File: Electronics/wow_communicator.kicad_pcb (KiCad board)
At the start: 2 copper layers, 5 parts, among them SW1 SW_SPST, SW2 SW_SPST, U1 STM32C011F6Px

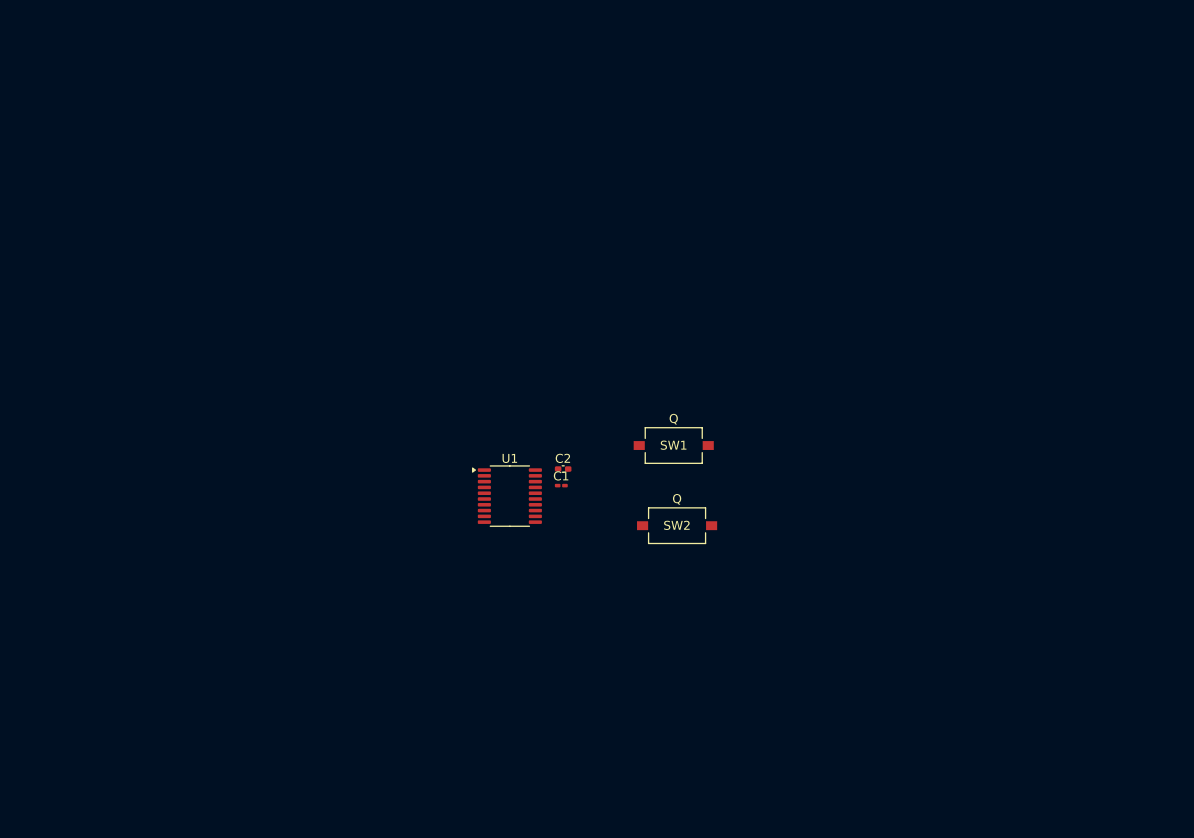
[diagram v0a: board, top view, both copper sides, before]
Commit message: arranged keys for keyboard. marked out lcd
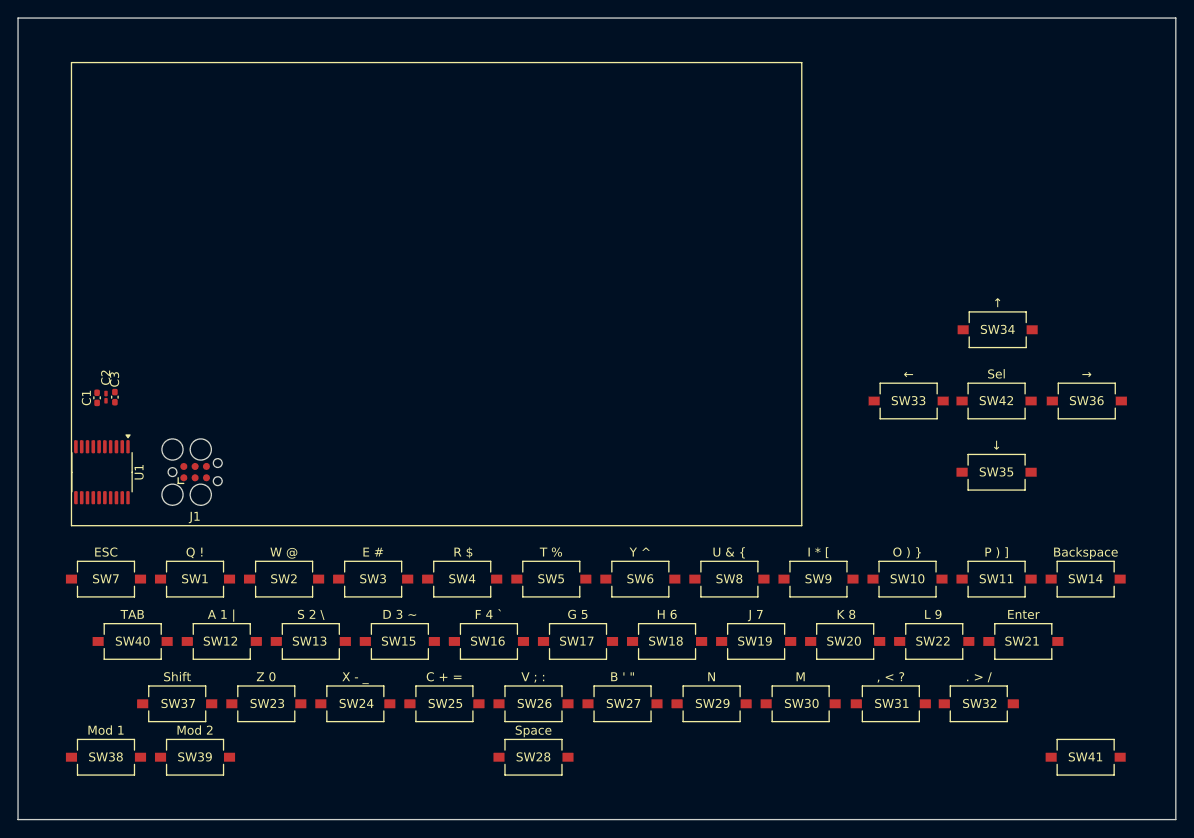
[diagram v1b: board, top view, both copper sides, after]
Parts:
- added C1: 100n, Capacitor_SMD:C_0402_1005Metric_Pad0.74x0.62mm_HandSolder, F.Cu at (93.9, 92.6)
- added J1: DEBUG, Connector:Tag-Connect_TC2030-IDC-FP_2x03_P1.27mm_Vertical, F.Cu at (104.9, 101.0)
- added SW10: SW_SPST, Button_Switch_SMD:SW_Tactile_SPST_NO_Straight_CK_PTS636Sx25SMTRLFS, F.Cu at (184.9, 113.0)
- added SW11: SW_SPST, Button_Switch_SMD:SW_Tactile_SPST_NO_Straight_CK_PTS636Sx25SMTRLFS, F.Cu at (194.9, 113.0)
- added SW12: SW_SPST, Button_Switch_SMD:SW_Tactile_SPST_NO_Straight_CK_PTS636Sx25SMTRLFS, F.Cu at (107.9, 120.0)
- added SW13: SW_SPST, Button_Switch_SMD:SW_Tactile_SPST_NO_Straight_CK_PTS636Sx25SMTRLFS, F.Cu at (117.9, 120.0)
- added SW14: SW_SPST, Button_Switch_SMD:SW_Tactile_SPST_NO_Straight_CK_PTS636Sx25SMTRLFS, F.Cu at (204.9, 113.0)
- added SW15: SW_SPST, Button_Switch_SMD:SW_Tactile_SPST_NO_Straight_CK_PTS636Sx25SMTRLFS, F.Cu at (127.9, 120.0)
- added SW16: SW_SPST, Button_Switch_SMD:SW_Tactile_SPST_NO_Straight_CK_PTS636Sx25SMTRLFS, F.Cu at (137.9, 120.0)
- added SW17: SW_SPST, Button_Switch_SMD:SW_Tactile_SPST_NO_Straight_CK_PTS636Sx25SMTRLFS, F.Cu at (147.9, 120.0)
- added SW18: SW_SPST, Button_Switch_SMD:SW_Tactile_SPST_NO_Straight_CK_PTS636Sx25SMTRLFS, F.Cu at (157.9, 120.0)
- added SW19: SW_SPST, Button_Switch_SMD:SW_Tactile_SPST_NO_Straight_CK_PTS636Sx25SMTRLFS, F.Cu at (167.9, 120.0)
- added SW20: SW_SPST, Button_Switch_SMD:SW_Tactile_SPST_NO_Straight_CK_PTS636Sx25SMTRLFS, F.Cu at (177.9, 120.0)
- added SW21: SW_SPST, Button_Switch_SMD:SW_Tactile_SPST_NO_Straight_CK_PTS636Sx25SMTRLFS, F.Cu at (197.9, 120.0)
- added SW22: SW_SPST, Button_Switch_SMD:SW_Tactile_SPST_NO_Straight_CK_PTS636Sx25SMTRLFS, F.Cu at (187.9, 120.0)
- added SW23: SW_SPST, Button_Switch_SMD:SW_Tactile_SPST_NO_Straight_CK_PTS636Sx25SMTRLFS, F.Cu at (112.9, 127.0)
- added SW24: SW_SPST, Button_Switch_SMD:SW_Tactile_SPST_NO_Straight_CK_PTS636Sx25SMTRLFS, F.Cu at (122.9, 127.0)
- added SW25: SW_SPST, Button_Switch_SMD:SW_Tactile_SPST_NO_Straight_CK_PTS636Sx25SMTRLFS, F.Cu at (132.9, 127.0)
- added SW26: SW_SPST, Button_Switch_SMD:SW_Tactile_SPST_NO_Straight_CK_PTS636Sx25SMTRLFS, F.Cu at (142.9, 127.0)
- added SW27: SW_SPST, Button_Switch_SMD:SW_Tactile_SPST_NO_Straight_CK_PTS636Sx25SMTRLFS, F.Cu at (152.9, 127.0)
- added SW28: SW_SPST, Button_Switch_SMD:SW_Tactile_SPST_NO_Straight_CK_PTS636Sx25SMTRLFS, F.Cu at (142.9, 133.0)
- added SW29: SW_SPST, Button_Switch_SMD:SW_Tactile_SPST_NO_Straight_CK_PTS636Sx25SMTRLFS, F.Cu at (162.9, 127.0)
- added SW3: SW_SPST, Button_Switch_SMD:SW_Tactile_SPST_NO_Straight_CK_PTS636Sx25SMTRLFS, F.Cu at (124.9, 113.0)
- added SW30: SW_SPST, Button_Switch_SMD:SW_Tactile_SPST_NO_Straight_CK_PTS636Sx25SMTRLFS, F.Cu at (172.9, 127.0)
- added SW31: SW_SPST, Button_Switch_SMD:SW_Tactile_SPST_NO_Straight_CK_PTS636Sx25SMTRLFS, F.Cu at (183.0, 127.0)
- added SW32: SW_SPST, Button_Switch_SMD:SW_Tactile_SPST_NO_Straight_CK_PTS636Sx25SMTRLFS, F.Cu at (192.9, 127.0)
- added SW33: SW_SPST, Button_Switch_SMD:SW_Tactile_SPST_NO_Straight_CK_PTS636Sx25SMTRLFS, F.Cu at (185.0, 93.0)
- added SW34: SW_SPST, Button_Switch_SMD:SW_Tactile_SPST_NO_Straight_CK_PTS636Sx25SMTRLFS, F.Cu at (195.0, 85.0)
- added SW35: SW_SPST, Button_Switch_SMD:SW_Tactile_SPST_NO_Straight_CK_PTS636Sx25SMTRLFS, F.Cu at (194.9, 101.0)
- added SW36: SW_SPST, Button_Switch_SMD:SW_Tactile_SPST_NO_Straight_CK_PTS636Sx25SMTRLFS, F.Cu at (205.0, 93.0)
- added SW37: SW_SPST, Button_Switch_SMD:SW_Tactile_SPST_NO_Straight_CK_PTS636Sx25SMTRLFS, F.Cu at (102.9, 127.0)
- added SW38: SW_SPST, Button_Switch_SMD:SW_Tactile_SPST_NO_Straight_CK_PTS636Sx25SMTRLFS, F.Cu at (94.9, 133.0)
- added SW39: SW_SPST, Button_Switch_SMD:SW_Tactile_SPST_NO_Straight_CK_PTS636Sx25SMTRLFS, F.Cu at (104.9, 133.0)
- added SW4: SW_SPST, Button_Switch_SMD:SW_Tactile_SPST_NO_Straight_CK_PTS636Sx25SMTRLFS, F.Cu at (134.9, 113.0)
- added SW40: SW_SPST, Button_Switch_SMD:SW_Tactile_SPST_NO_Straight_CK_PTS636Sx25SMTRLFS, F.Cu at (97.9, 120.0)
- added SW41: SW_SPST, Button_Switch_SMD:SW_Tactile_SPST_NO_Straight_CK_PTS636Sx25SMTRLFS, F.Cu at (204.9, 133.0)
- added SW42: SW_SPST, Button_Switch_SMD:SW_Tactile_SPST_NO_Straight_CK_PTS636Sx25SMTRLFS, F.Cu at (194.9, 93.0)
- added SW5: SW_SPST, Button_Switch_SMD:SW_Tactile_SPST_NO_Straight_CK_PTS636Sx25SMTRLFS, F.Cu at (144.9, 113.0)
- added SW6: SW_SPST, Button_Switch_SMD:SW_Tactile_SPST_NO_Straight_CK_PTS636Sx25SMTRLFS, F.Cu at (154.9, 113.0)
- added SW7: SW_SPST, Button_Switch_SMD:SW_Tactile_SPST_NO_Straight_CK_PTS636Sx25SMTRLFS, F.Cu at (94.9, 113.0)
- added SW8: SW_SPST, Button_Switch_SMD:SW_Tactile_SPST_NO_Straight_CK_PTS636Sx25SMTRLFS, F.Cu at (164.9, 113.0)
- added SW9: SW_SPST, Button_Switch_SMD:SW_Tactile_SPST_NO_Straight_CK_PTS636Sx25SMTRLFS, F.Cu at (174.9, 113.0)
- moved SW1 54.5 mm to (104.9, 113.0)
- moved C2 52.1 mm to (94.9, 92.6), turned to 90 degrees
- moved C3 51.0 mm to (95.9, 92.6), turned to 90 degrees
- moved SW2 46.2 mm to (114.9, 113.0)
- moved U1 45.9 mm to (94.4, 101.0), turned to -90 degrees
- renumbered C1 to C2, C2 to C3, SW2 to SW1, SW1 to SW2
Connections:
- SW1 pad 1: unconnected-(SW2-A-Pad1) -> Net-(SW1-A)
- SW1 pad 2: unconnected-(SW2-B-Pad2) -> Net-(SW1-B)
- SW2 pad 1: unconnected-(SW1-A-Pad1) -> Net-(SW1-A)
- SW2 pad 2: unconnected-(SW1-B-Pad2) -> Net-(SW16-B)
- U1 pad 1: unconnected-(U1-PB7-Pad1) -> Net-(SW12-B)
- U1 pad 10: unconnected-(U1-PA3-Pad10) -> Net-(SW15-A)
- U1 pad 11: unconnected-(U1-PA4-Pad11) -> Net-(SW11-B)
- U1 pad 12: unconnected-(U1-PA5-Pad12) -> Net-(SW10-B)
- U1 pad 13: unconnected-(U1-PA6-Pad13) -> Net-(SW16-B)
- U1 pad 14: unconnected-(U1-PA7-Pad14) -> Net-(SW1-B)
- U1 pad 15: unconnected-(U1-PA8-Pad15) -> Net-(SW1-A)
- U1 pad 16: unconnected-(U1-PA9/PA11-Pad16) -> /keyboard_matrix/KEYBOARD_SCL
- U1 pad 17: unconnected-(U1-PA10/PA12-Pad17) -> /keyboard_matrix/KEYBOARD_SDA
- U1 pad 18: unconnected-(U1-PA13-Pad18) -> /keyboard_matrix/DEBUG_SWDIO
- U1 pad 19: unconnected-(U1-PA14-Pad19) -> /keyboard_matrix/DEBUG_SWCLK
- U1 pad 2: unconnected-(U1-PC14-Pad2) -> Net-(SW13-B)
- U1 pad 20: unconnected-(U1-PB6-Pad20) -> Net-(SW10-A)
- U1 pad 3: unconnected-(U1-PC15-Pad3) -> Net-(SW14-B)
- U1 pad 7: unconnected-(U1-PA0-Pad7) -> Net-(SW36-A)
- U1 pad 8: unconnected-(U1-PA1-Pad8) -> Net-(SW29-A)
- U1 pad 9: unconnected-(U1-PA2-Pad9) -> Net-(SW22-A)
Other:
- board outline added: 130 x 90 mm
- copper layers 2 -> 4

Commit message: basic power supply layout some minor design notes. charge ic likely to change. possibly bridge out fuel gague
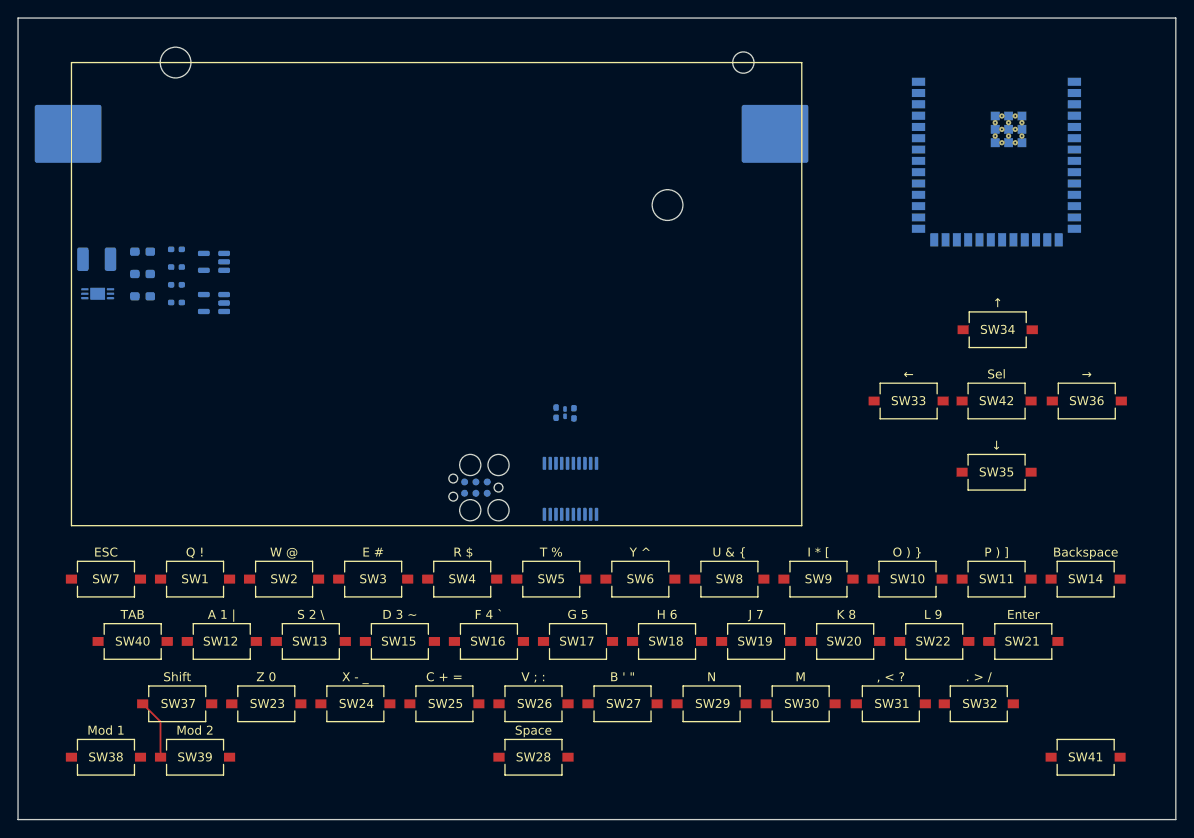
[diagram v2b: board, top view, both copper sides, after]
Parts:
- added BT1: 18650, Battery:BatteryHolder_Keystone_1042_1x18650, B.Cu at (130.3, 63.0)
- added C4: 1u, Capacitor_SMD:C_0603_1608Metric_Pad1.08x0.95mm_HandSolder, B.Cu at (99.0, 76.2)
- added C5: 10u, Capacitor_SMD:C_0603_1608Metric_Pad1.08x0.95mm_HandSolder, B.Cu at (99.0, 78.7)
- added C6: 10u, Capacitor_SMD:C_0603_1608Metric_Pad1.08x0.95mm_HandSolder, B.Cu at (99.0, 81.2)
- added R1: 100m, Resistor_SMD:R_1210_3225Metric_Pad1.30x2.65mm_HandSolder, B.Cu at (93.8, 77.1)
- added R4: 2k, Resistor_SMD:R_0402_1005Metric_Pad0.72x0.64mm_HandSolder, B.Cu at (102.8, 76.0)
- added R5: 5.1k, Resistor_SMD:R_0402_1005Metric_Pad0.72x0.64mm_HandSolder, B.Cu at (102.8, 78.0)
- added R6: 5.1k, Resistor_SMD:R_0402_1005Metric_Pad0.72x0.64mm_HandSolder, B.Cu at (102.8, 80.0)
- added R7: 1M, Resistor_SMD:R_0402_1005Metric_Pad0.72x0.64mm_HandSolder, B.Cu at (102.8, 81.9)
- added U2: ESP32-S3-WROOM-2, RF_Module:ESP32-S3-WROOM-2, B.Cu at (194.9, 62.4)
- added U3: TLV75733PDBV, Package_TO_SOT_SMD:SOT-23-5, B.Cu at (107.0, 77.4)
- added U4: LTC2942, Package_DFN_QFN:DFN-6-1EP_3x2mm_P0.5mm_EP1.65x1.35mm, B.Cu at (93.9, 81.0)
- added U5: MCP73812T-435I-OT, Package_TO_SOT_SMD:SOT-23-5, B.Cu at (107.0, 82.0)
- C1, C2, C3, J1, U1: moved to B.Cu
- moved C1 53.6 mm to (147.4, 94.4)
- moved U1 52.6 mm to (147.0, 102.9)
- moved C2 51.6 mm to (146.4, 94.3)
- moved C3 49.6 mm to (145.4, 94.3)
- moved J1 31.6 mm to (136.4, 102.7), turned to 180 degrees
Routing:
- net Net-(SW36-A): track 0.00 -> 6.83 mm
